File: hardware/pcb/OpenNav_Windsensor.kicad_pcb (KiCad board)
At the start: 2 copper layers, 40 x 40 mm, 11 parts, among them IC1 AS5600-ASOT, J1 Conn_01x02_Pin, U1 XIAO-ESP32-C6, U2 StpDwnE3.3-0.5, U3 SS411P, U4 DS18B20

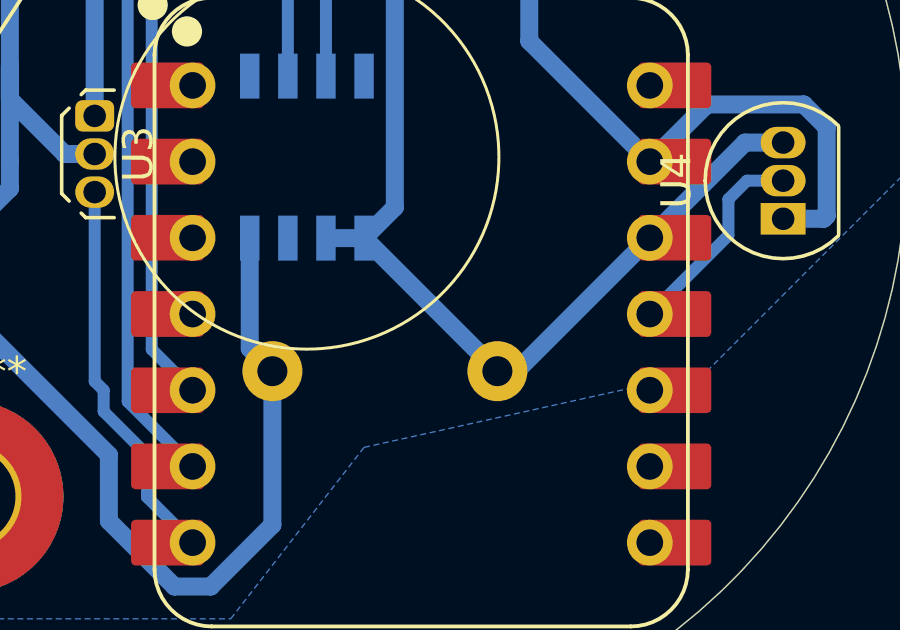
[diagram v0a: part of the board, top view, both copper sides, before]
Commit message: Corrected capacitor size based on what bought
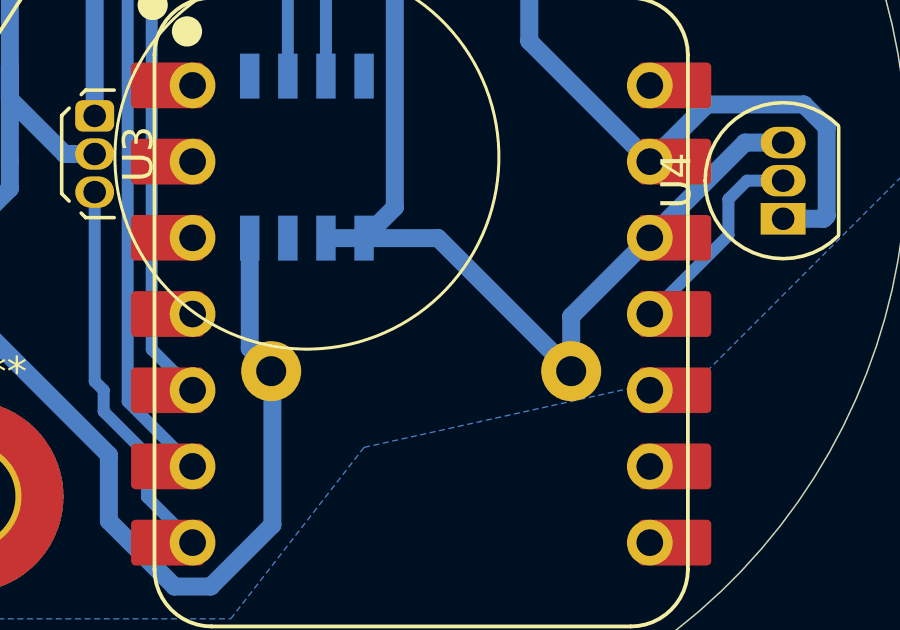
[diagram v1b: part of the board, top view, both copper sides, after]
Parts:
- C3: footprint Capacitor_THT:C_Disc_D8.0mm_W5.0mm_P7.50mm -> Capacitor_THT:C_Disc_D7.5mm_W5.0mm_P10.00mm
- moved C3 2.46 mm to (141.5, 64.1)
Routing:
- net +3.3V: track 64.2 -> 65.3 mm
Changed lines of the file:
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@@
 		)
 	)
-	(footprint "Capacitor_THT:C_Disc_D8.0mm_W5.0mm_P7.50mm"
-		(layer "B.Cu")
-		(at 139.065 64.135 180)
-		(descr "C, Disc series, Radial, pin pitch=7.50mm, diameter*width=8*5.0mm^2, Capacitor, http://www.vishay.com/docs/28535/vy2series.pdf")
-		(tags "C Disc series Radial pin pitch 7.50mm diameter 8mm width 5.0mm Capacitor")
+	(footprint "Capacitor_THT:C_Disc_D7.5mm_W5.0mm_P10.00mm"
+		(layer "B.Cu")
+		(at 141.525 64.135 180)
+		(descr "C, Disc series, Radial, pin pitch=10.00mm, diameter*width=7.5*5.0mm^2, Capacitor, http://www.vishay.com/docs/28535/vy2series.pdf")
+		(tags "C Disc series Radial pin pitch 10.00mm diameter 7.5mm width 5.0mm Capacitor")
 		(property "Reference" "C3"
-			(at 3.75 3.75 0)
+			(at 5 3.75 0)
 			(layer "B.SilkS")
 			(effects
@@
 		)
 		(property "Value" "100nF"
-			(at 3.75 -3.75 0)
+			(at 5 -3.75 0)
 			(layer "B.Fab")
 			(effects
@@
 		(attr through_hole)
 		(fp_line
-			(start 7.87 2.62)
-			(end 7.87 1.184)
-			(stroke
-				(width 0.12)
-				(type solid)
-			)
-			(layer "B.SilkS")
-		)
-		(fp_line
-			(start 7.87 -1.184)
-			(end 7.87 -2.62)
-			(stroke
-				(width 0.12)
-				(type solid)
-			)
-			(layer "B.SilkS")
-		)
-		(fp_line
-			(start 7.87 -2.62)
-			(end -0.37 -2.62)
-			(stroke
-				(width 0.12)
-				(type solid)
-			)
-			(layer "B.SilkS")
-		)
-		(fp_line
-			(start -0.37 2.62)
-			(end 7.87 2.62)
-			(stroke
-				(width 0.12)
-				(type solid)
-			)
-			(layer "B.SilkS")
-		)
-		(fp_line
-			(start -0.37 1.184)
-			(end -0.37 2.62)
-			(stroke
-				(width 0.12)
-				(type solid)
-			)
-			(layer "B.SilkS")
-		)
-		(fp_line
-			(start -0.37 -2.62)
-			(end -0.37 -1.184)
+			(start 8.87 2.62)
+			(end 8.87 0.511)
+			(stroke
+				(width 0.12)
+				(type solid)
+			)
+			(layer "B.SilkS")
+		)
+		(fp_line
+			(start 8.87 -0.511)
+			(end 8.87 -2.62)
+			(stroke
+				(width 0.12)
+				(type solid)
+			)
+			(layer "B.SilkS")
+		)
+		(fp_line
+			(start 8.87 -2.62)
+			(end 1.13 -2.62)
+			(stroke
+				(width 0.12)
+				(type solid)
+			)
+			(layer "B.SilkS")
+		)
+		(fp_line
+			(start 1.13 2.62)
+			(end 8.87 2.62)
+			(stroke
+				(width 0.12)
+				(type solid)
+			)
+			(layer "B.SilkS")
+		)
+		(fp_line
+			(start 1.13 0.511)
+			(end 1.13 2.62)
+			(stroke
+				(width 0.12)
+				(type solid)
+			)
+			(layer "B.SilkS")
+		)
+		(fp_line
+			(start 1.13 -2.62)
+			(end 1.13 -0.511)
 			(stroke
 				(width 0.12)
@@
 		(fp_rect
 			(start -1.25 2.75)
-			(end 8.75 -2.75)
+			(end 11.25 -2.75)
 			(stroke
 				(width 0.05)
@@
 		)
 		(fp_rect
-			(start -0.25 2.5)
-			(end 7.75 -2.5)
+			(start 1.25 2.5)
+			(end 8.75 -2.5)
 			(stroke
 				(width 0.1)
@@
 		)
 		(fp_text user "${REFERENCE}"
-			(at 3.75 0 0)
+			(at 5 0 0)
 			(layer "B.Fab")
 			(effects
@@
 		)
 		(pad "2" thru_hole circle
-			(at 7.5 0 180)
+			(at 10 0 180)
 			(size 2 2)
 			(drill 1)
@@
 		)
 		(embedded_fonts no)
-		(model "${KICAD9_3DMODEL_DIR}/Capacitor_THT.3dshapes/C_Disc_D8.0mm_W5.0mm_P7.50mm.step"
+		(model "${KICAD9_3DMODEL_DIR}/Capacitor_THT.3dshapes/C_Disc_D7.5mm_W5.0mm_P10.00mm.step"
 			(offset
 				(xyz 0 0 0)
@@
 	)
 	(segment
-		(start 139.065 64.135)
-		(end 139.7 64.135)
-		(width 0.6)
-		(layer "B.Cu")
-		(net 1)
-	)
-	(segment
 		(start 128.905 40.005)
 		(end 132.715 40.005)
@@
 	)
 	(segment
-		(start 134.62 59.7)
-		(end 134.63 59.7)
+		(start 141.525 62.31)
+		(end 144.145 59.69)
 		(width 0.6)
 		(layer "B.Cu")
@@
 	)
 	(segment
+		(start 141.525 64.135)
+		(end 141.525 62.31)
+		(width 0.6)
+		(layer "B.Cu")
+		(net 1)
+	)
+	(segment
 		(start 125.641 49.977488)
 		(end 125.641 55.626)
@@
 	)
 	(segment
+		(start 137.09 59.7)
+		(end 141.525 64.135)
+		(width 0.6)
+		(layer "B.Cu")
+		(net 1)
+	)
+	(segment
 		(start 123.395023 45.514977)
 		(end 128.905 40.005)
@@
 	)
 	(segment
-		(start 134.63 59.7)
-		(end 139.065 64.135)
+		(start 134.62 59.7)
+		(end 137.09 59.7)
 		(width 0.6)
 		(layer "B.Cu")
@@
 		(width 0.6)
 		(layer "B.Cu")
-		(net 1)
-	)
-	(segment
-		(start 139.7 64.135)
-		(end 144.145 59.69)
-		(width 0.6)
-		(layer "B.Cu")
